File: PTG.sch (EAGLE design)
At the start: 86 parts, among them IC1 TPS62120, IC2 PIC32MK1024MCF064-I_PT, IC3 LT1762EMS8-5PBF, IC4 TPS561208DDCR, IC5 LT1762EMS8-5PBF, J1 STX-3100-5N, J2 RCJ-01X_PHONO_SINGLE, U4 PCM1748E/2K, X1 22-23-2041

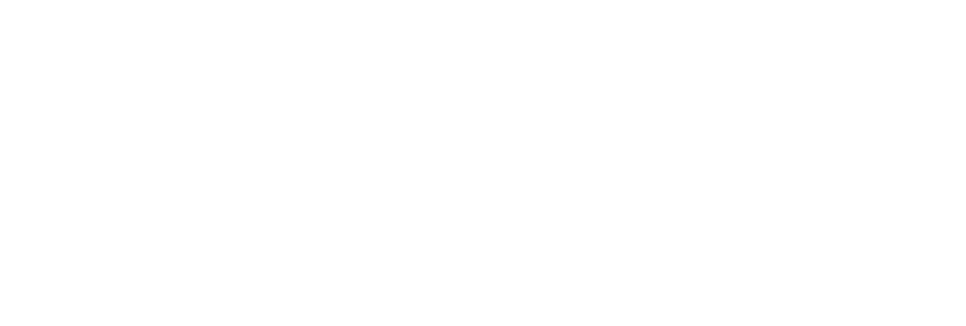
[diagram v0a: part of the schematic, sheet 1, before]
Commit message: Add project personnel to schematic
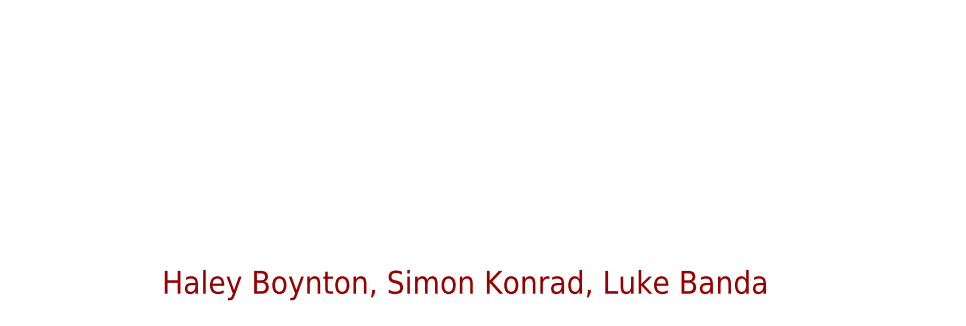
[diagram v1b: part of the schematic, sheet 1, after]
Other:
- note added: "Haley Boynton, Simon Konrad, Luke Banda"
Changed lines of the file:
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@@
 <sheet>
 <plain>
+<text x="119.38" y="-96.52" size="2.54" layer="94">Haley Boynton, Simon Konrad, Luke Banda</text>
 </plain>
 <instances>

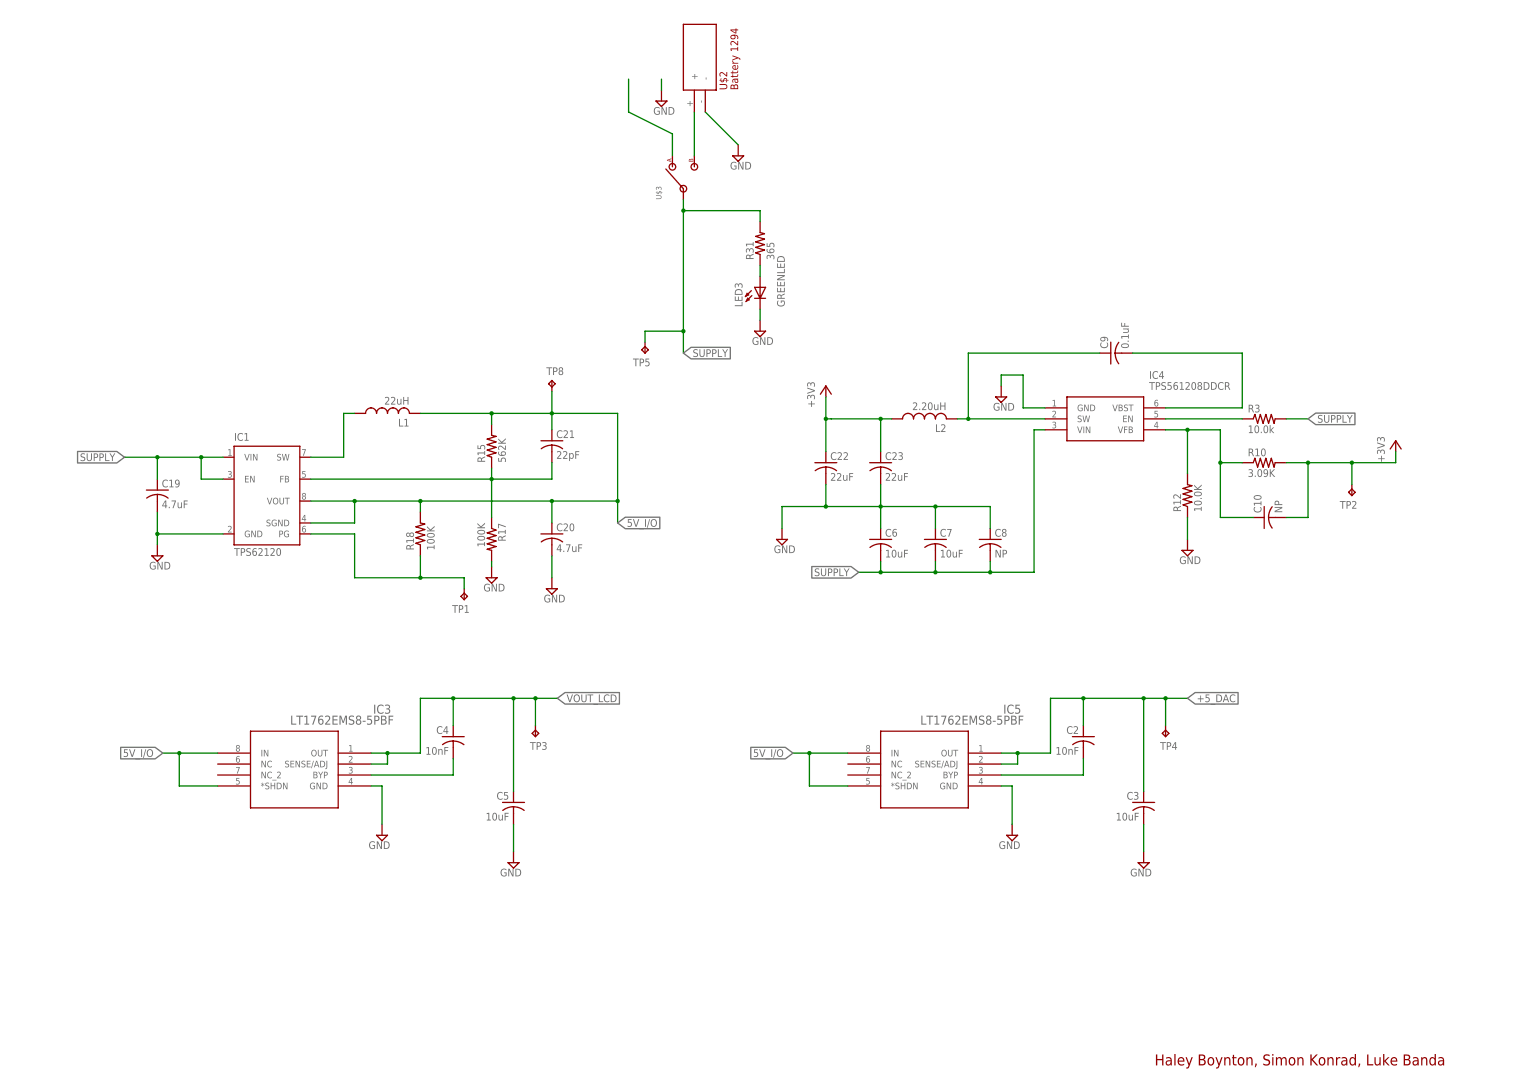
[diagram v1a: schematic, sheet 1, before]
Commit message: Minor changes to schematic, added LDO traces, added DAC traces, added power traces
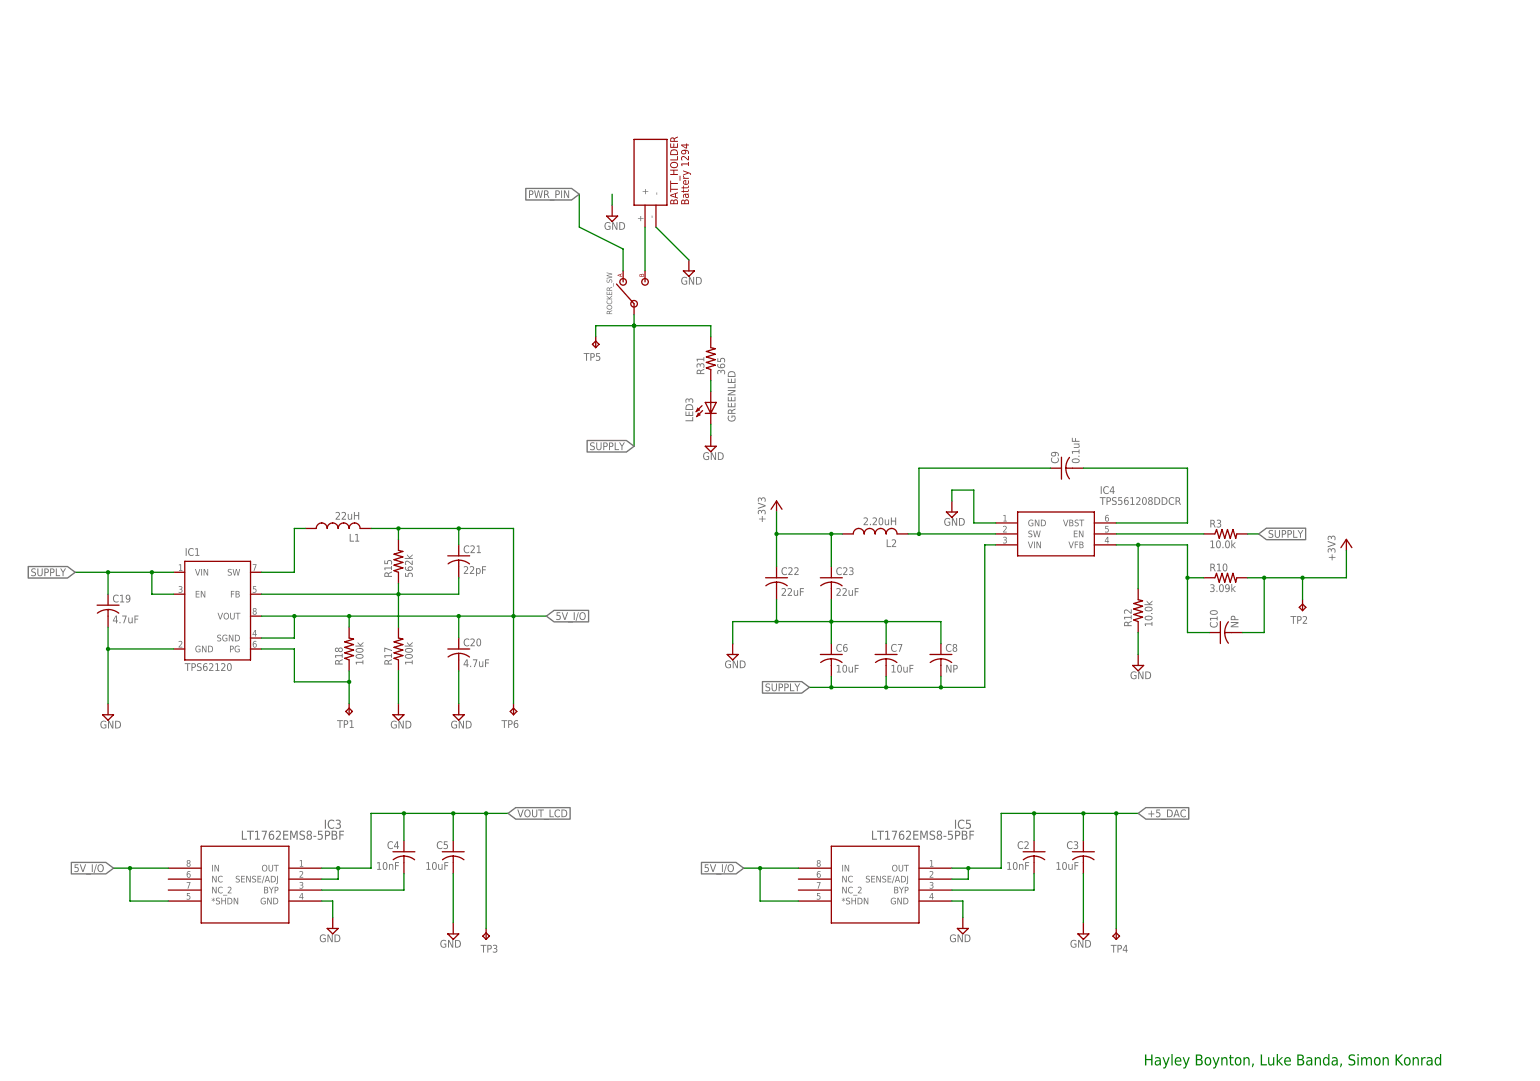
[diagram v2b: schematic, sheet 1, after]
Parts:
- removed TP8: TPTP20SQ, testpad:TPTP20SQ
- removed U$2: BATTERY_HOLDER, BattHolder:BATTERY_HOLDER
- removed U$3: POWERSWITCH, RockerSwitch:POWERSWITCH
- added BATT_HOLDER: BATTERY_HOLDER, BattHolder:BATTERY_HOLDER
- added ROCKER_SW: POWERSWITCH, RockerSwitch:POWERSWITCH
- added TP6: TPTP20SQ, testpad:TPTP20SQ
- R1: value 1.00K -> 1.00k
- R10: value 3.09K -> 3.09k
- R12, R13, R14, R7: value 10.0K -> 10.0k
- R15: value 562K -> 562k
- R17, R18: value 100K -> 100k
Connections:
- net ADD_TEST_PAD renamed PWRGOOD
- removed net N$1 (its old number): U$2.+, U$3.3
- removed net PWR_PINS: U$3.1
- new net PWR_PIN: ROCKER_SW.1
- new net SW-B: BATT_HOLDER.+, ROCKER_SW.3
- net 5V_I/O: now also TP6.TP; no longer TP8.TP
- net GND: now also BATT_HOLDER.-, R17.1; no longer R17.2, U$2.-
- net N$11: now also IC2.AN15/CVD15/RPE15/FLT8/PMPA0/PSPA0/RE15, R11.1; no longer LED2.+, R9.1
- net N$12: now also R11.2; no longer R11.1
- net N$15: now also LED2.+, R9.2; no longer IC2.AN15/CVD15/RPE15/FLT8/PMPA0/PSPA0/RE15, R11.2
- net N$17: now also R9.1; no longer R9.2
- net N$8: now also R17.2; no longer R17.1
- net SUPPLY: now also ROCKER_SW.2; no longer U$3.2
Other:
- note added: "Hayley Boynton, Luke Banda, Simon Konrad"
- note removed: "Haley Boynton, Simon Konrad, Luke Banda"
- note removed: "Programming Jack for PIC"
- note removed: "Series Termination 133 Ohms"
- moved on the sheet: C1, C10, C11, C12, C13, C14, C15, C16, C17, C19, C2, C20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

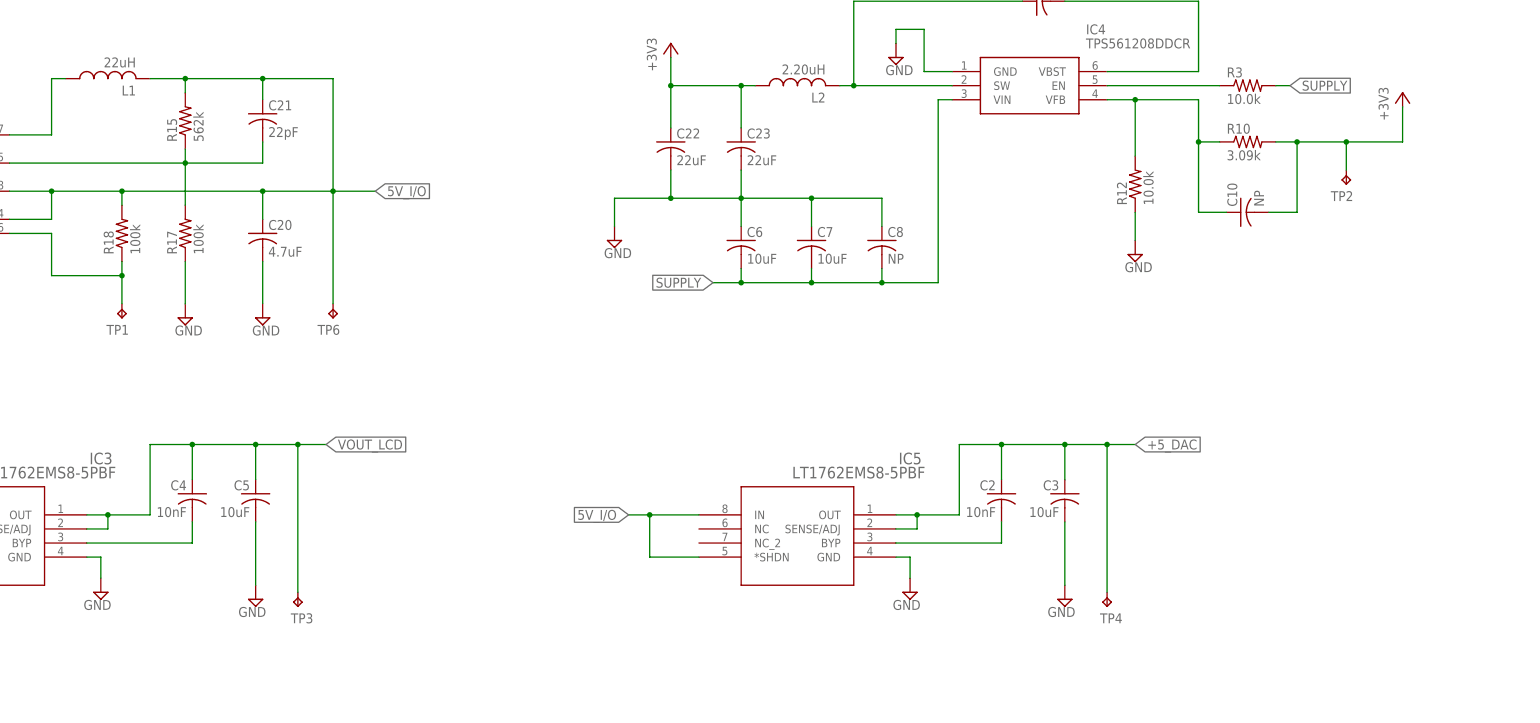
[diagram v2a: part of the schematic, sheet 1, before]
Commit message: minor fixes, switched DAC_ZEROL / DAC ZEROH pins, need new test pad package
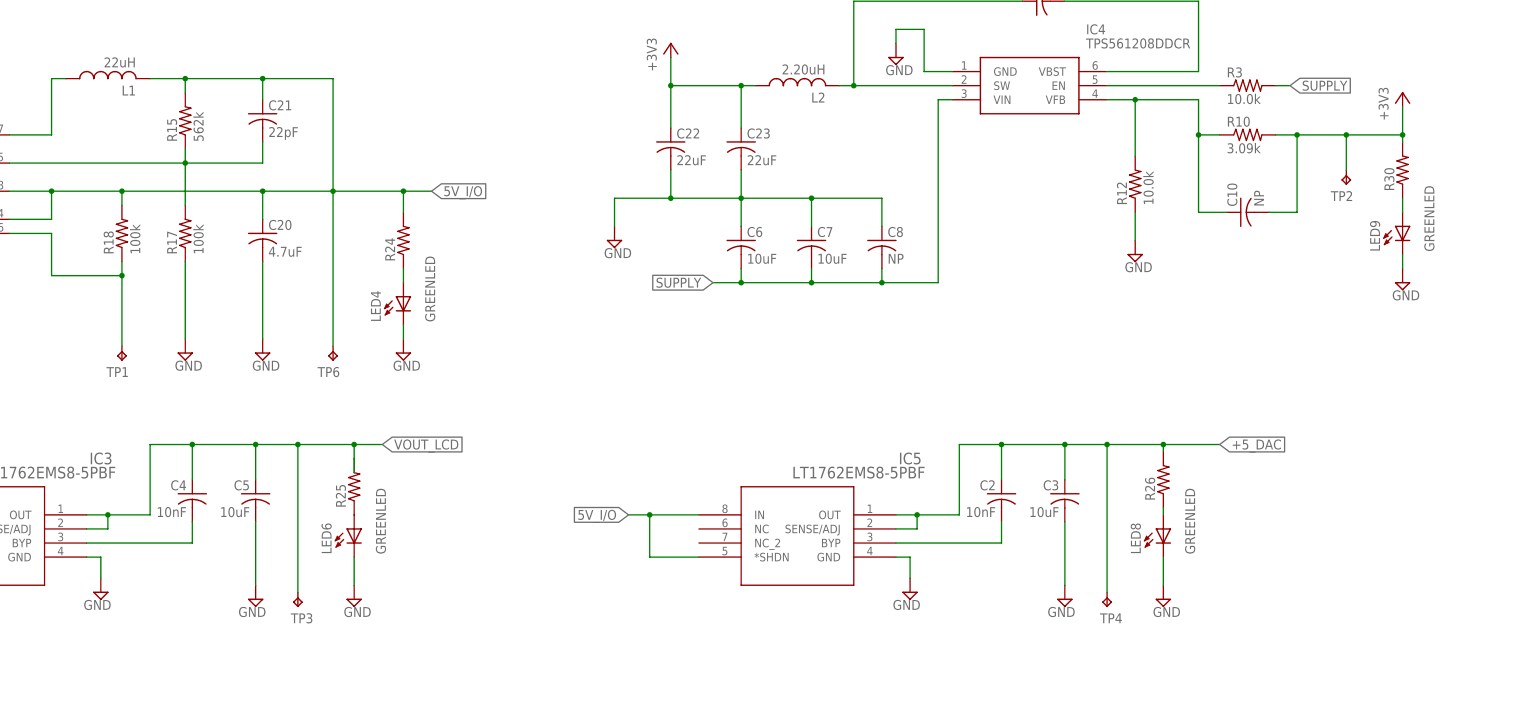
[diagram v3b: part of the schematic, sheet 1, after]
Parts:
- added LED4, LED6, LED8, LED9: GREENLED, GreenLED:GREENLED
- added R24, R25, R26, R30: (no value), resistor:R-US_R0603
- added TP7: TPTP20SQ, testpad:TPTP20SQ
- renumbered U$1 to DIS1, U$8 to Y1
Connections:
- new net N$22: LED4.+, R24.1
- new net N$24: LED6.+, R25.1
- new net N$26: LED8.+, R26.1
- new net N$28: LED9.+, R30.1
- net +3V3: now also R30.2
- net +5_DAC: now also R26.2
- net 5V_I/O: now also R24.2
- net DAC_DATA: now also TP7.TP
- net DAC_ZEROH: now also IC2.AN19/CVD19/RPG6/PMPA5/RG6; no longer IC2.AN18/CVD18/RPG7/PMPA4/RG7
- net DAC_ZEROL: now also IC2.AN18/CVD18/RPG7/PMPA4/RG7; no longer IC2.AN19/CVD19/RPG6/PMPA5/RG6
- net GND: now also LED4.-, LED6.-, LED8.-, LED9.-
- net VOUT_LCD: now also R25.2
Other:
- moved on the sheet: R10, TP1, TP6
